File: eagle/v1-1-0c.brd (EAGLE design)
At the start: 313 x 132.9 mm, 180 parts, among them J1 CR22A-44D-2.54DSA(70), J3 26-60-4040, J4 AUDIO_JACK_3.5MM_PTH, J5 DIN5, SW1 3PDT-AQ-SWITCH, SW2 9077-1, U10 7805, U11 74LS10N, U13 74LS04N, U14 4528N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

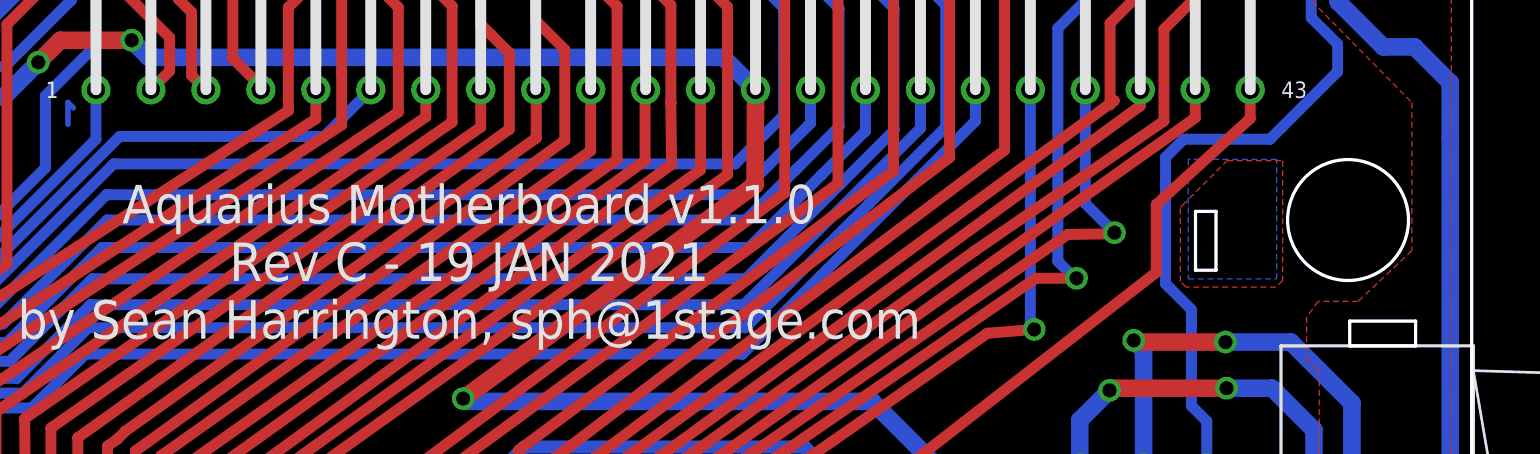
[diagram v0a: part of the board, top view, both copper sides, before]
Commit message: Layout update
Fix a positioning problem with right cartridge port alignment/screw hole.
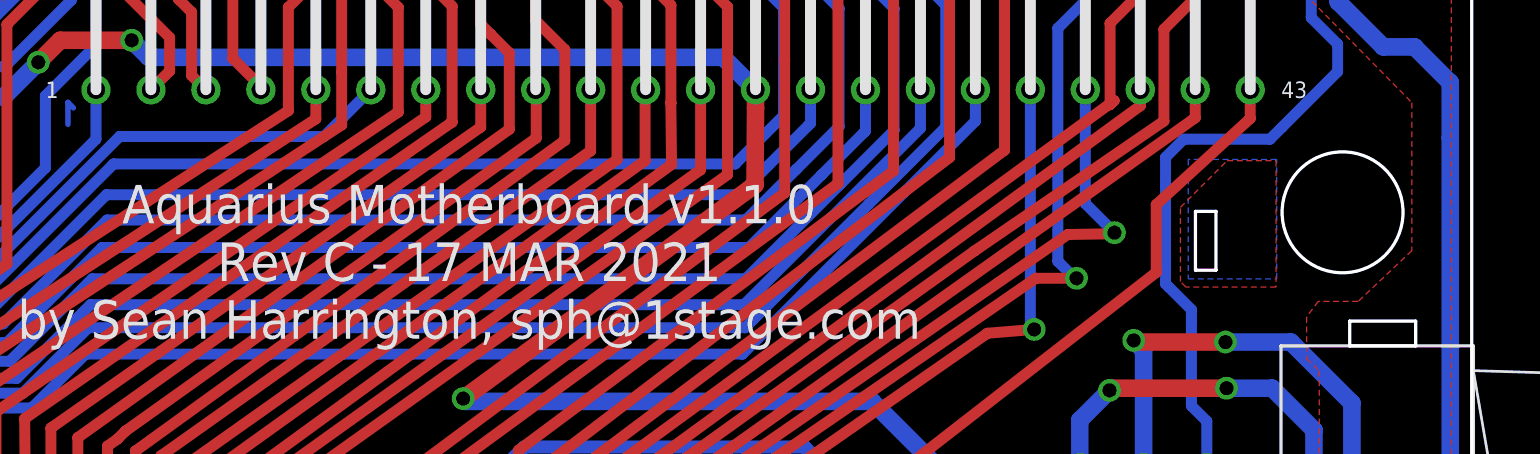
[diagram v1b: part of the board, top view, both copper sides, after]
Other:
- outline, holes or cut-outs redrawn
- board text added: "Aquarius Motherboard v1.1.0 Rev C - 17 MAR 2021 by Sean Harrington, sph@1stage.com"
- board text removed: "Aquarius Motherboard v1.1.0 Rev C - 19 JAN 2021 by Sean Harrington, sph@1stage.com"

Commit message: Correct input voltages on PSU for schematic
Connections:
- net PIN-8.8VDC renamed PIN+8.8VDC
- removed net PIN-16VDC: C42.1, J3.4, L5.1
- new net PIN+16VDC: C41.1, J3.1, L8.1
- net PIN-19VDC: now also C42.1, J3.4, L5.1; no longer C41.1, J3.1, L8.1
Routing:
- net PIN-16VDC: track 42.3 -> 0.00 mm
- net PIN+16VDC: track 0.00 -> 25.9 mm
- net PIN-19VDC: track 25.9 -> 42.3 mm
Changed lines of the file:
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@@
 <wire x1="186.0296" y1="92.837" x2="191.897" y2="92.837" width="0.508" layer="16"/>
 </signal>
-<signal name="PIN-8.8VDC">
+<signal name="PIN+8.8VDC">
 <wire x1="42.3418" y1="123.2154" x2="40.767" y2="124.7902" width="0.8128" layer="16"/>
 <wire x1="40.767" y1="124.7902" x2="27.6606" y2="124.7902" width="0.8128" layer="16"/>
@@
 <wire x1="22.606" y1="128.4986" x2="26.3144" y2="124.7902" width="0.8128" layer="16"/>
 </signal>
-<signal name="PIN-19VDC">
+<signal name="PIN+16VDC">
 <wire x1="52.5272" y1="131.445" x2="45.6438" y2="131.445" width="0.8128" layer="16"/>
 <wire x1="42.316403125" y1="131.445" x2="45.6438" y2="131.445" width="0.8128" layer="16"/>
@@
 <wire x1="36.4236" y1="95.631" x2="36.4236" y2="119.9134" width="0.8128" layer="1"/>
 </signal>
-<signal name="PIN-16VDC">
+<signal name="PIN-19VDC">
 <contactref element="C42" pad="1"/>
 <contactref element="L5" pad="1"/>
